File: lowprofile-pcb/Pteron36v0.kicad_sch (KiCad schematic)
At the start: 46 parts, among them J1 AudioJack4, J2 AudioJack4, SW10 SW_PUSH, SW12 SW_PUSH, SW13 SW_PUSH, SW14 SW_PUSH, SW15 SW_PUSH, SW17 SW_PUSH, SW18 SW_PUSH, SW19 SW_PUSH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

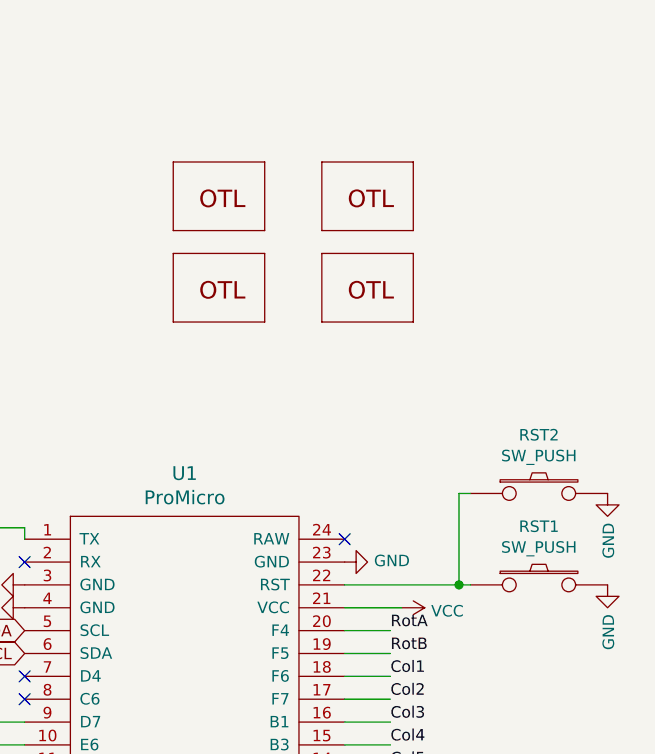
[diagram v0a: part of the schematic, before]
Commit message: introduce the snapable pcb with 4 config of keyboard possible
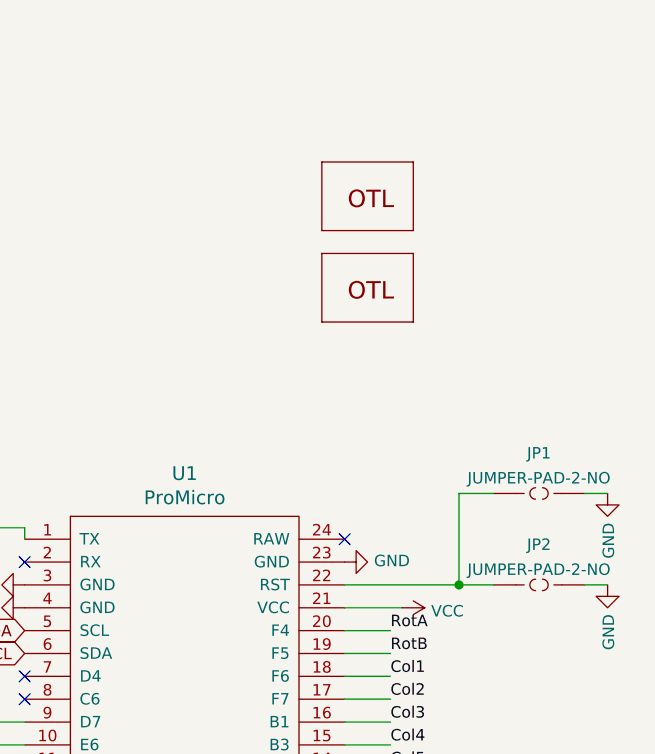
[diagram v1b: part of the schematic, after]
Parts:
- removed LOGO1, LOGO2: LOGO-OTL, personal-logo:miryoku-kicad-small, symbol SparkFun-Aesthetics:LOGO-OTL
- removed RST1, RST2: SW_PUSH, acheron_Hardware:smdPushBtn, symbol keyboard_parts:SW_PUSH
- added JP1, JP2: JUMPER-PAD-2-NO, Jumper:SolderJumper-2_P1.3mm_Open_Pad1.0x1.5mm, symbol SparkFun-Passives:JUMPER-PAD-2-NO
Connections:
- net GND: now also JP1.2, JP2.2
- net at U1.22 (RST): now also JP1.1, JP2.1
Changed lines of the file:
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@@
     (stroke (width 0) (type solid) (color 0 0 0 0))
   )
-  (wire (pts (xy 261.62 110.49) (xy 262.89 110.49))
+  (wire (pts (xy 261.62 110.49) (xy 265.43 110.49))
     (stroke (width 0) (type solid) (color 0 0 0 0))
   )
@@
     (stroke (width 0) (type solid) (color 0 0 0 0))
   )
-  (wire (pts (xy 261.62 120.65) (xy 262.89 120.65))
+  (wire (pts (xy 261.62 120.65) (xy 265.43 120.65))
+    (stroke (width 0) (type solid) (color 0 0 0 0))
+  )
+  (wire (pts (xy 275.59 110.49) (xy 278.13 110.49))
+    (stroke (width 0) (type solid) (color 0 0 0 0))
+  )
+  (wire (pts (xy 275.59 120.65) (xy 278.13 120.65))
     (stroke (width 0) (type solid) (color 0 0 0 0))
   )
@@
     (pin "1")
   )
+  (symbol (lib_id "SparkFun-Passives:JUMPER-PAD-2-NO") (at 270.51 110.49 0) (unit 1)
+    (in_bom yes) (on_board yes) (fields_autoplaced)
+    (property "Reference" "JP1" (id 0) (at 270.51 106.0154 0))
+    (property "Value" "JUMPER-PAD-2-NO" (id 1) (at 270.51 108.7905 0))
+    (property "Footprint" "Jumper:SolderJumper-2_P1.3mm_Open_Pad1.0x1.5mm" (id 2) (at 271.272 106.68 0)
+      (effects (font (size 0.508 0.508)) hide)
+    )
+    (property "Datasheet" "" (id 3) (at 270.51 110.49 0)
+      (effects (font (size 1.27 1.27)) hide)
+    )
+    (pin "1")
+    (pin "2")
+  )
+  (symbol (lib_id "SparkFun-Passives:JUMPER-PAD-2-NO") (at 270.51 120.65 0) (unit 1)
+    (in_bom yes) (on_board yes) (fields_autoplaced)
+    (property "Reference" "JP2" (id 0) (at 270.51 116.1754 0))
+    (property "Value" "JUMPER-PAD-2-NO" (id 1) (at 270.51 118.9505 0))
+    (property "Footprint" "Jumper:SolderJumper-2_P1.3mm_Open_Pad1.0x1.5mm" (id 2) (at 271.272 116.84 0)
+      (effects (font (size 0.508 0.508)) hide)
+    )
+    (property "Datasheet" "" (id 3) (at 270.51 120.65 0)
+      (effects (font (size 1.27 1.27)) hide)
+    )
+    (pin "1")
+    (pin "2")
+  )
   (symbol (lib_id "Diode:1N4148") (at 39.37 44.45 0) (unit 1)
     (in_bom yes) (on_board yes)
@@
     (pin "1")
     (pin "2")
-  )
-  (symbol (lib_id "keyboard_parts:SW_PUSH") (at 270.51 110.49 0) (unit 1)
-    (in_bom yes) (on_board yes)
-    (property "Reference" "RST2" (id 0) (at 270.51 104.013 0))
-    (property "Value" "SW_PUSH" (id 1) (at 270.51 106.3244 0))
-    (property "Footprint" "acheron_Hardware:smdPushBtn" (id 2) (at 270.51 110.49 0)
-      (effects (font (size 1.524 1.524)) hide)
-    )
-    (property "Datasheet" "" (id 3) (at 270.51 110.49 0)
-      (effects (font (size 1.524 1.524)))
-    )
-    (pin "1")
-    (pin "2")
-  )
-  (symbol (lib_id "keyboard_parts:SW_PUSH") (at 270.51 120.65 0) (unit 1)
-    (in_bom yes) (on_board yes)
-    (property "Reference" "RST1" (id 0) (at 270.51 114.173 0))
-    (property "Value" "SW_PUSH" (id 1) (at 270.51 116.4844 0))
-    (property "Footprint" "acheron_Hardware:smdPushBtn" (id 2) (at 270.51 120.65 0)
-      (effects (font (size 1.524 1.524)) hide)
-    )
-    (property "Datasheet" "" (id 3) (at 270.51 120.65 0)
-      (effects (font (size 1.524 1.524)))
-    )
-    (pin "1")
-    (pin "2")
-  )
-  (symbol (lib_id "SparkFun-Aesthetics:LOGO-OTL") (at 234.95 76.2 0) (unit 1)
-    (in_bom yes) (on_board yes)
-    (property "Reference" "LOGO1" (id 0) (at 234.95 76.2 0)
-      (effects (font (size 1.27 1.27)) hide)
-    )
-    (property "Value" "LOGO-OTL" (id 1) (at 234.95 76.2 0)
-      (effects (font (size 1.27 1.27)) hide)
-    )
-    (property "Footprint" "personal-logo:miryoku-kicad-small" (id 2) (at 235.712 72.39 0)
-      (effects (font (size 0.508 0.508)) hide)
-    )
-    (property "Datasheet" "" (id 3) (at 234.95 76.2 0)
-      (effects (font (size 1.27 1.27)) hide)
-    )
-  )
-  (symbol (lib_id "SparkFun-Aesthetics:LOGO-OTL") (at 234.95 86.36 0) (unit 1)
-    (in_bom yes) (on_board yes)
-    (property "Reference" "LOGO2" (id 0) (at 234.95 86.36 0)
-      (effects (font (size 1.27 1.27)) hide)
-    )
-    (property "Value" "LOGO-OTL" (id 1) (at 234.95 86.36 0)
-      (effects (font (size 1.27 1.27)) hide)
-    )
-    (property "Footprint" "personal-logo:miryoku-kicad-small" (id 2) (at 235.712 82.55 0)
-      (effects (font (size 0.508 0.508)) hide)
-    )
-    (property "Datasheet" "" (id 3) (at 234.95 86.36 0)
-      (effects (font (size 1.27 1.27)) hide)
-    )
   )
   (symbol (lib_id "SparkFun-Aesthetics:LOGO-OTL") (at 251.46 76.2 0) (unit 1)
@@
       (reference "J2") (unit 1) (value "AudioJack4") (footprint "Keebio-Parts:TRRS-PJ-320A")
     )
-    (path "/00000000-0000-0000-0000-0000607a2bee"
-      (reference "LOGO1") (unit 1) (value "LOGO-OTL") (footprint "personal-logo:miryoku-kicad-small")
-    )
-    (path "/00000000-0000-0000-0000-0000607a2653"
-      (reference "LOGO2") (unit 1) (value "LOGO-OTL") (footprint "personal-logo:miryoku-kicad-small")
+    (path "/0b76a048-da1d-4d10-82af-9264c0605235"
+      (reference "JP1") (unit 1) (value "JUMPER-PAD-2-NO") (footprint "Jumper:SolderJumper-2_P1.3mm_Open_Pad1.0x1.5mm")
+    )
+    (path "/c097909c-92c1-4c73-bddc-504d7eb669e6"
+      (reference "JP2") (unit 1) (value "JUMPER-PAD-2-NO") (footprint "Jumper:SolderJumper-2_P1.3mm_Open_Pad1.0x1.5mm")
     )
     (path "/e4d4d865-3cb1-431d-b18c-3cc2928a93c9"
@@
       (reference "LOGO4") (unit 1) (value "LOGO-OTL") (footprint "personal-logo:peacock-medium")
     )
-    (path "/00000000-0000-0000-0000-0000607b81a2"
-      (reference "RST1") (unit 1) (value "SW_PUSH") (footprint "acheron_Hardware:smdPushBtn")
-    )
-    (path "/00000000-0000-0000-0000-0000607e0b2f"
-      (reference "RST2") (unit 1) (value "SW_PUSH") (footprint "acheron_Hardware:smdPushBtn")
-    )
     (path "/00000000-0000-0000-0000-000060963566"
